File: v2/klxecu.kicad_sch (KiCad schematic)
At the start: 65 parts, among them IC1 SP721, J1 Conn_02x18_Odd_Even, J2 Conn_01x02, J3 Conn_02x04_Counter_Clockwise, J4 Conn_01x01_Male, Q1 2N6517, Q2 STP62NS04Z, Q3 STP62NS04Z, Q4 STP62NS04Z, Q5 STP62NS04Z, Q6 STP62NS04Z, Q7 STP62NS04Z, U1 mega_2560_pro, U2 ERZ-V14D220, U3 LM340T-5.0, U4 ATtiny84-20P, U5 74LS14DR, U6 TC4422AVPA

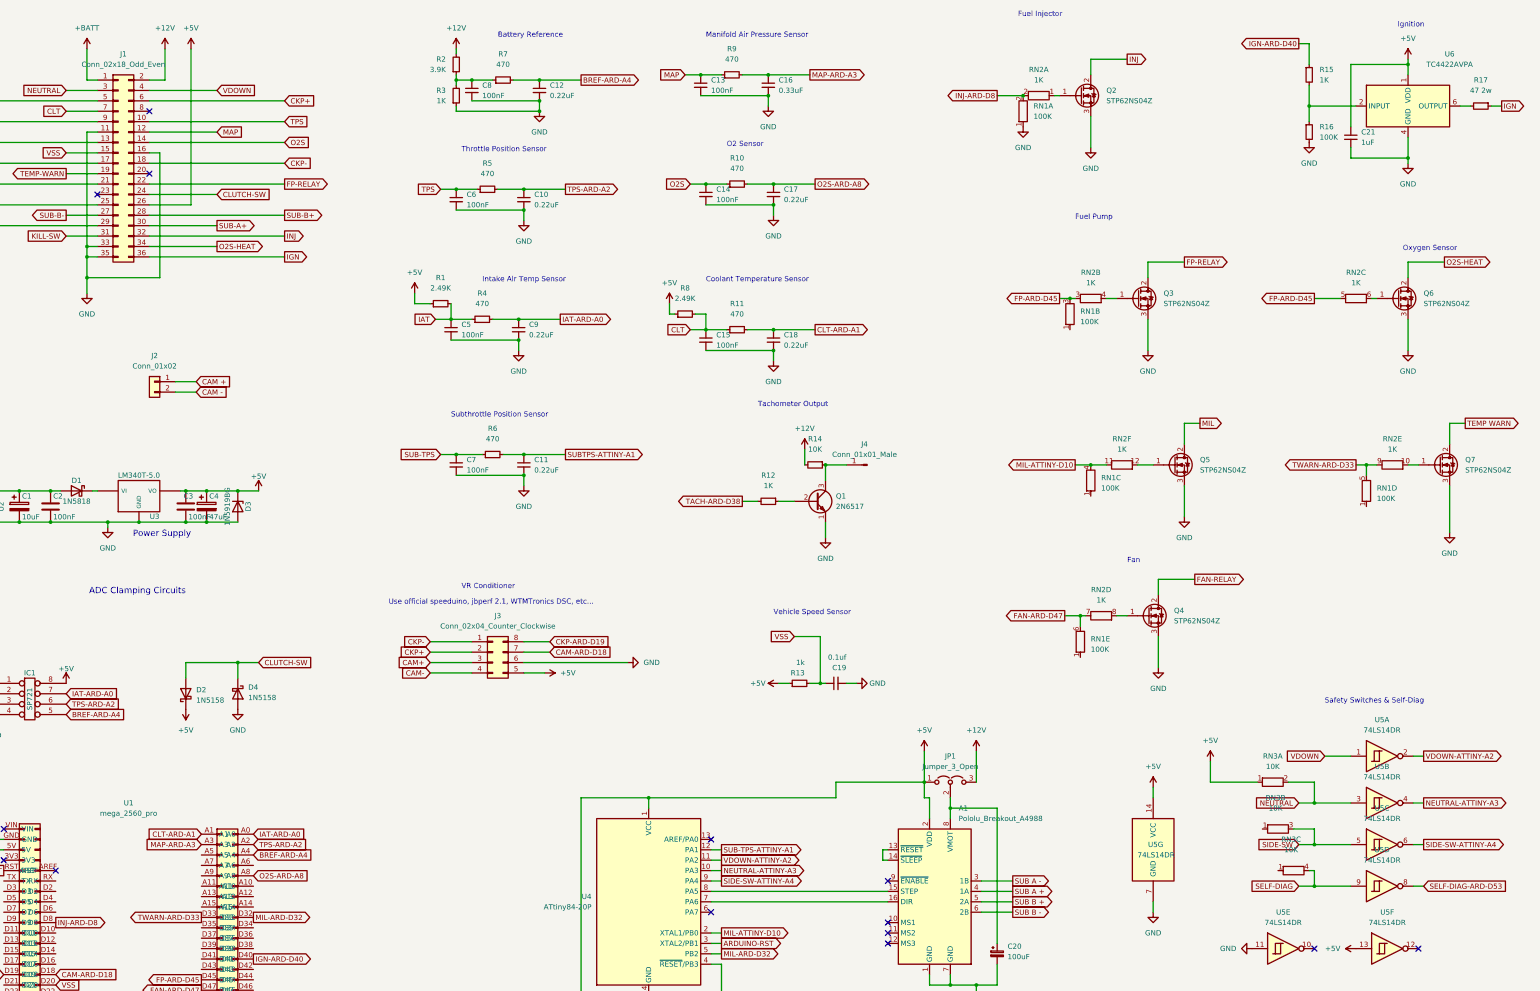
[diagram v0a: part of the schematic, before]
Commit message: Change low current transistors to SMT
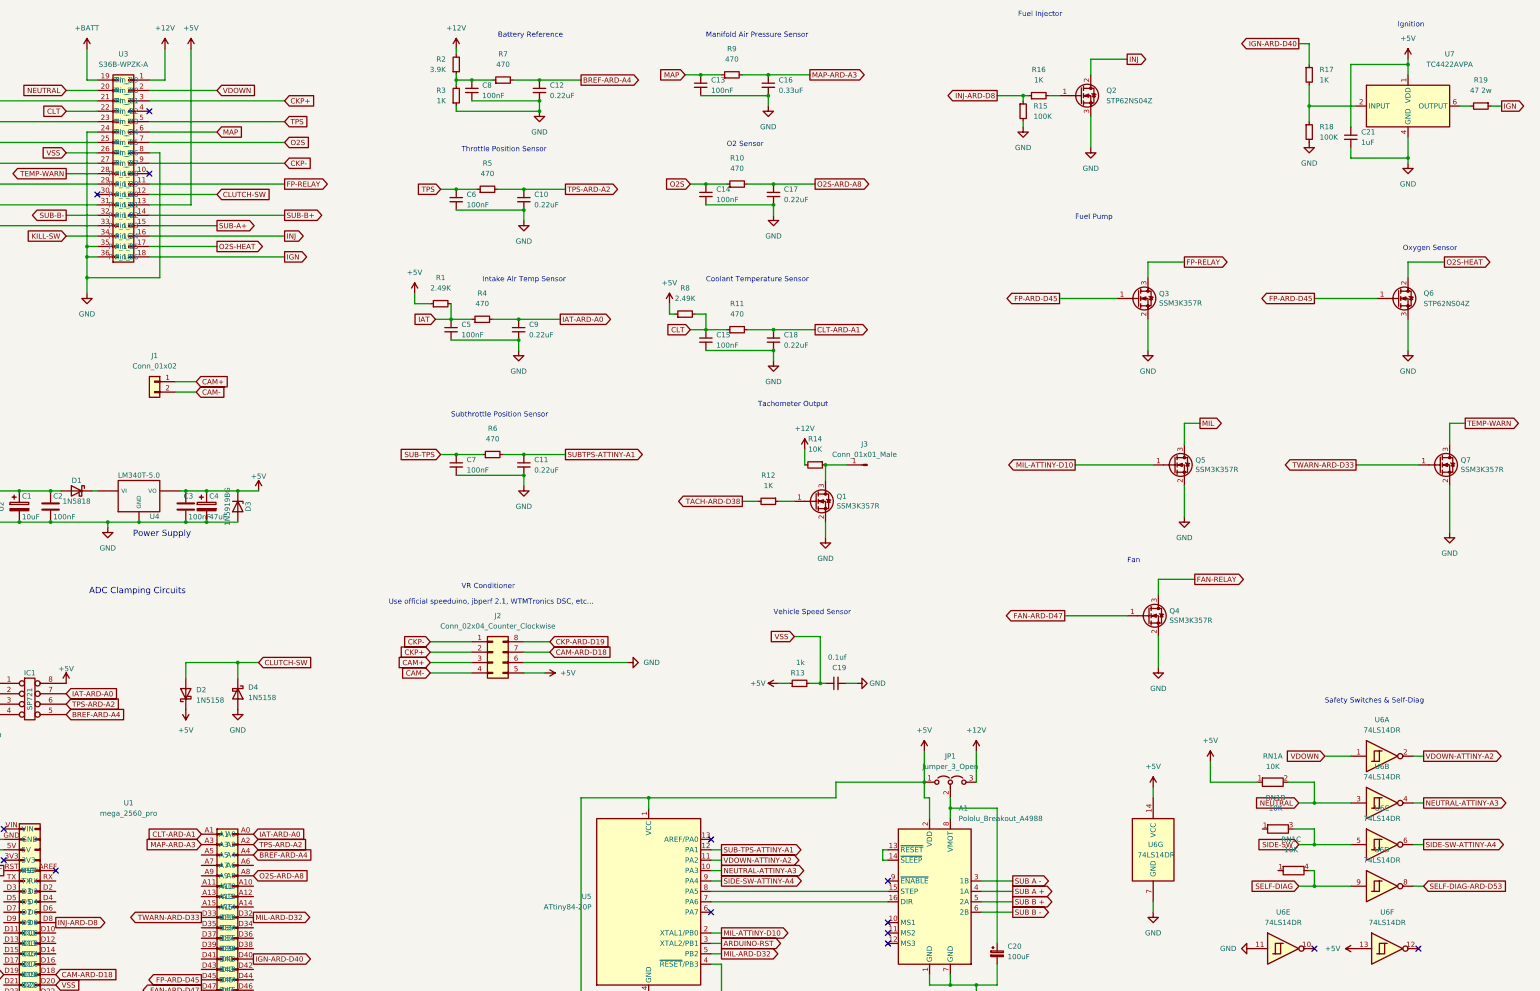
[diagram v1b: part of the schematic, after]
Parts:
- removed J1: Conn_02x18_Odd_Even, Connector_PinHeader_2.54mm:PinHeader_2x18_P2.54mm_Vertical, symbol Connector_Generic:Conn_02x18_Odd_Even
- removed Q1: 2N6517, Package_TO_SOT_THT:TO-92_Inline, symbol Transistor_BJT:2N3904
- removed Q3, Q4, Q5, Q7: STP62NS04Z, Package_TO_SOT_THT:TO-220-3_Vertical, symbol Transistor_FET:BUZ11
- removed RN1: 100K, Resistor_THT:R_Array_SIP6, symbol Device:R_Network05_Split
- removed RN2: 1K, Resistor_THT:R_Array_SIP12, symbol Device:R_Pack06_SIP_Split
- added Q1, Q3, Q4, Q5, Q7: SSM3K357R, Package_TO_SOT_SMD:SOT-23, symbol Transistor_FET:2N7002
- added R15: 100K, Resistor_SMD:R_0805_2012Metric, symbol Device:R_Small
- added R16: 1K, Resistor_SMD:R_0805_2012Metric, symbol Device:R_Small
- added U3: S36B-WPZK-A, mega_2560:S36B-WPZK-A, symbol mega_2560:S36B-WPZK-A
- renumbered J2 to J1, J3 to J2, J4 to J3, R15 to R17, R16 to R18, R17 to R19, RN3 to RN1, U3 to U4, U4 to U5, U5 to U6, U6 to U7
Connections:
- net CAM + is gone; now on net CAM+: J1.1 (Pin_1)
- net CAM - is gone; now on net CAM-: J1.2 (Pin_2)
- net +12V: now also U3.1 (Pin_1)
- net +5V: now also U3.13 (Pin_13)
- net +BATT: now also U3.19 (Pin_19)
- net CKP+: now also U3.3 (Pin_3)
- net CKP-: now also U3.9 (Pin_9)
- net CLT: now also U3.22 (Pin_22)
- net CLUTCH-SW: now also U3.12 (Pin_12)
- net FAN-ARD-D47: now also Q4.1 (G)
- net FAN-RELAY: now also Q4.3 (D), U3.33 (Pin_33)
- net FP-ARD-D45: now also Q6.1 (G), Q3.1 (G)
- net FP-RELAY: now also Q3.3 (D), U3.11 (Pin_11)
- net GND: now also Q1.2 (S), Q3.2 (S), Q4.2 (S), Q5.2 (S), Q7.2 (S), R15.2, U3.24 (Pin_24), U3.35 (Pin_35), U3.36 (Pin_36), U3.8 (Pin_8)
- net IAT: now also U3.25 (Pin_25)
- net IGN: now also U3.18 (Pin_18)
- net INJ: now also U3.16 (Pin_16)
- net INJ-ARD-D8: now also R15.1, R16.1
- net KILL-SW: now also U3.34 (Pin_34)
- net MAP: now also U3.6 (Pin_6)
- net MIL: now also Q5.3 (D), U3.21 (Pin_21)
- net MIL-ATTINY-D10: now also Q5.1 (G)
- net NEUTRAL: now also U3.20 (Pin_20)
- net O2S: now also U3.7 (Pin_7)
- net O2S-HEAT: now also U3.17 (Pin_17)
- net SELF-DIAG: now also U3.23 (Pin_23)
- net SIDE-SW: now also U3.29 (Pin_29)
- net SUB-A+: now also U3.15 (Pin_15)
- net SUB-A-: now also U3.31 (Pin_31)
- net SUB-B+: now also U3.14 (Pin_14)
- net SUB-B-: now also U3.32 (Pin_32)
- net SUB-TPS: now also U3.27 (Pin_27)
- net TEMP-WARN: now also Q7.3 (D), U3.28 (Pin_28)
- net TPS: now also U3.5 (Pin_5)
- net TWARN-ARD-D33: now also Q7.1 (G)
- net VDOWN: now also U3.2 (Pin_2)
- net VSS: now also U3.26 (Pin_26)
- net at J3.1 (Pin_1), R14.1: now also Q1.3 (D)
- net at R12.1: now also Q1.1 (G)
- net at Q2.1 (G): now also R16.2

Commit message: add silkscreen outline for VR conditioner module
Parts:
- J2: footprint Package_DIP:DIP-8_W7.62mm_Socket -> mega_2560:vr_conditioner
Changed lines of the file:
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@@
     (property "Reference" "J2" (id 0) (at 156.21 163.83 0))
     (property "Value" "Conn_02x04_Counter_Clockwise" (id 1) (at 156.21 166.37 0))
-    (property "Footprint" "Package_DIP:DIP-8_W7.62mm_Socket" (id 2) (at 154.94 172.72 0)
+    (property "Footprint" "mega_2560:vr_conditioner" (id 2) (at 154.94 172.72 0)
       (effects (font (size 1.27 1.27)) hide)
     )
@@
     )
     (path "/a4646a71-a41a-457e-b69f-0409bde12e01"
-      (reference "J2") (unit 1) (value "Conn_02x04_Counter_Clockwise") (footprint "Package_DIP:DIP-8_W7.62mm_Socket")
+      (reference "J2") (unit 1) (value "Conn_02x04_Counter_Clockwise") (footprint "mega_2560:vr_conditioner")
     )
     (path "/7efd4165-947a-4227-b367-bffed70d4e31"

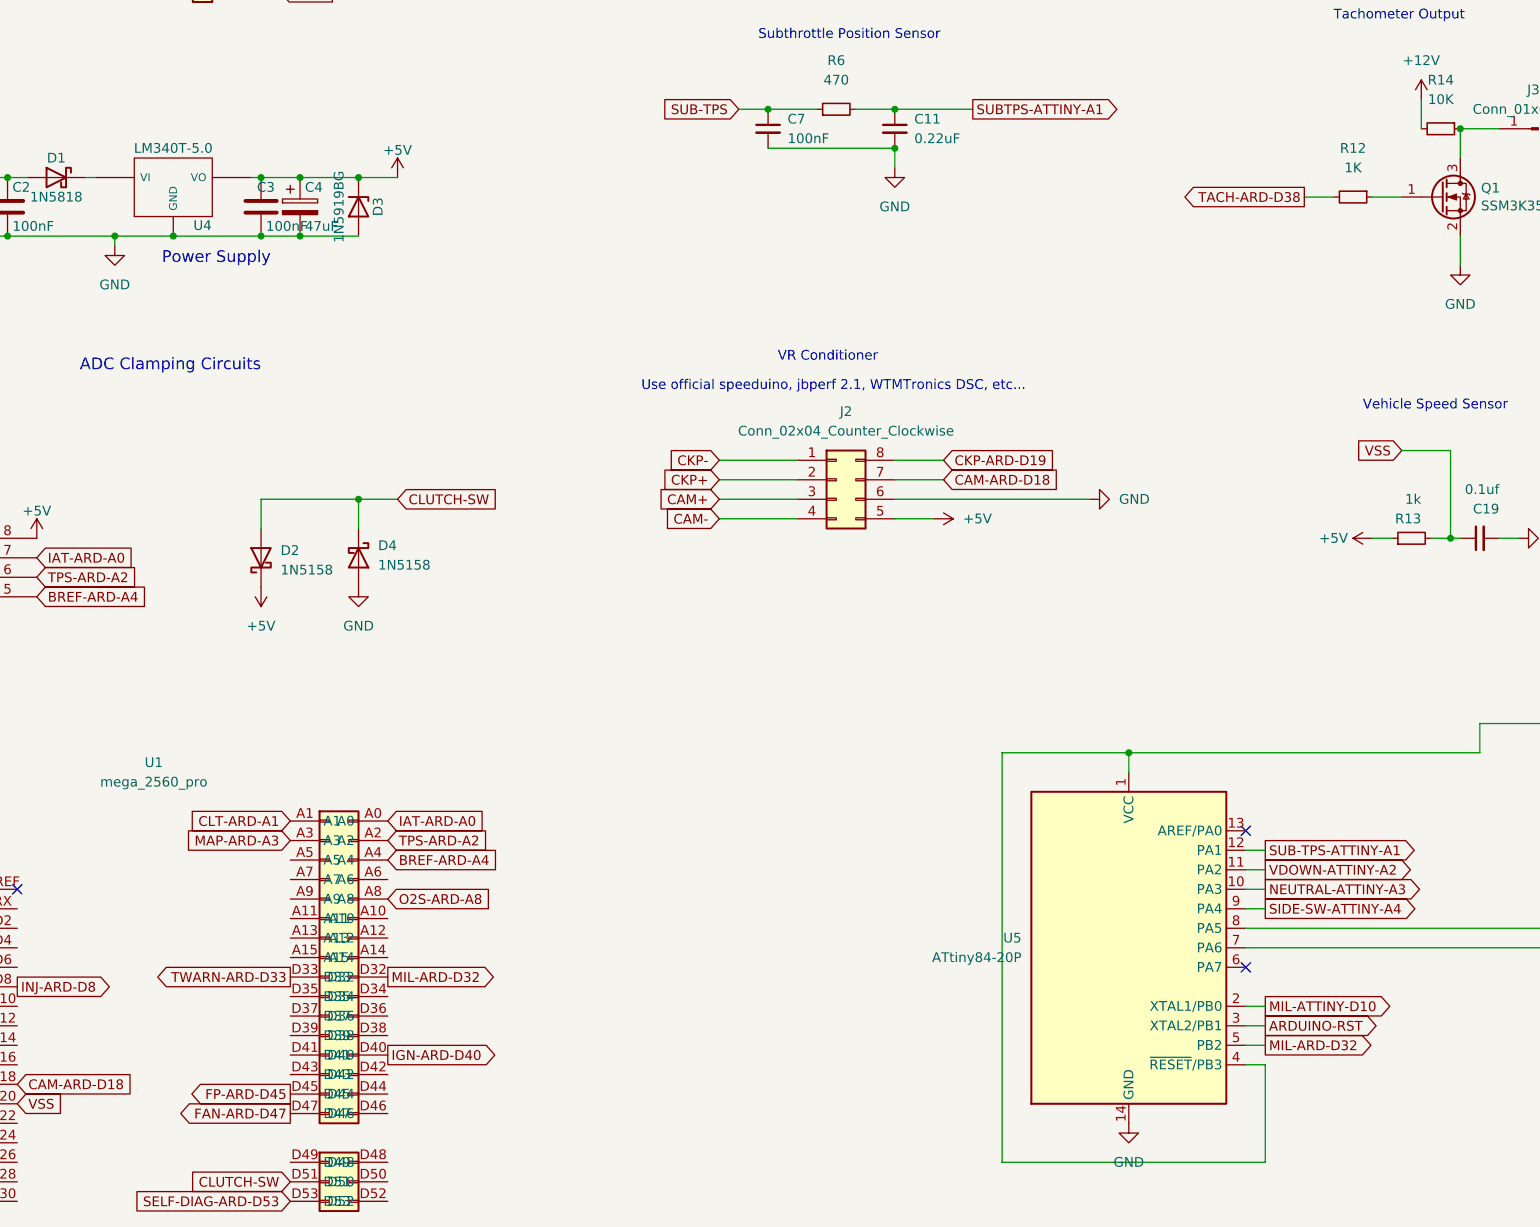
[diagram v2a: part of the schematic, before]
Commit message: fix tach output
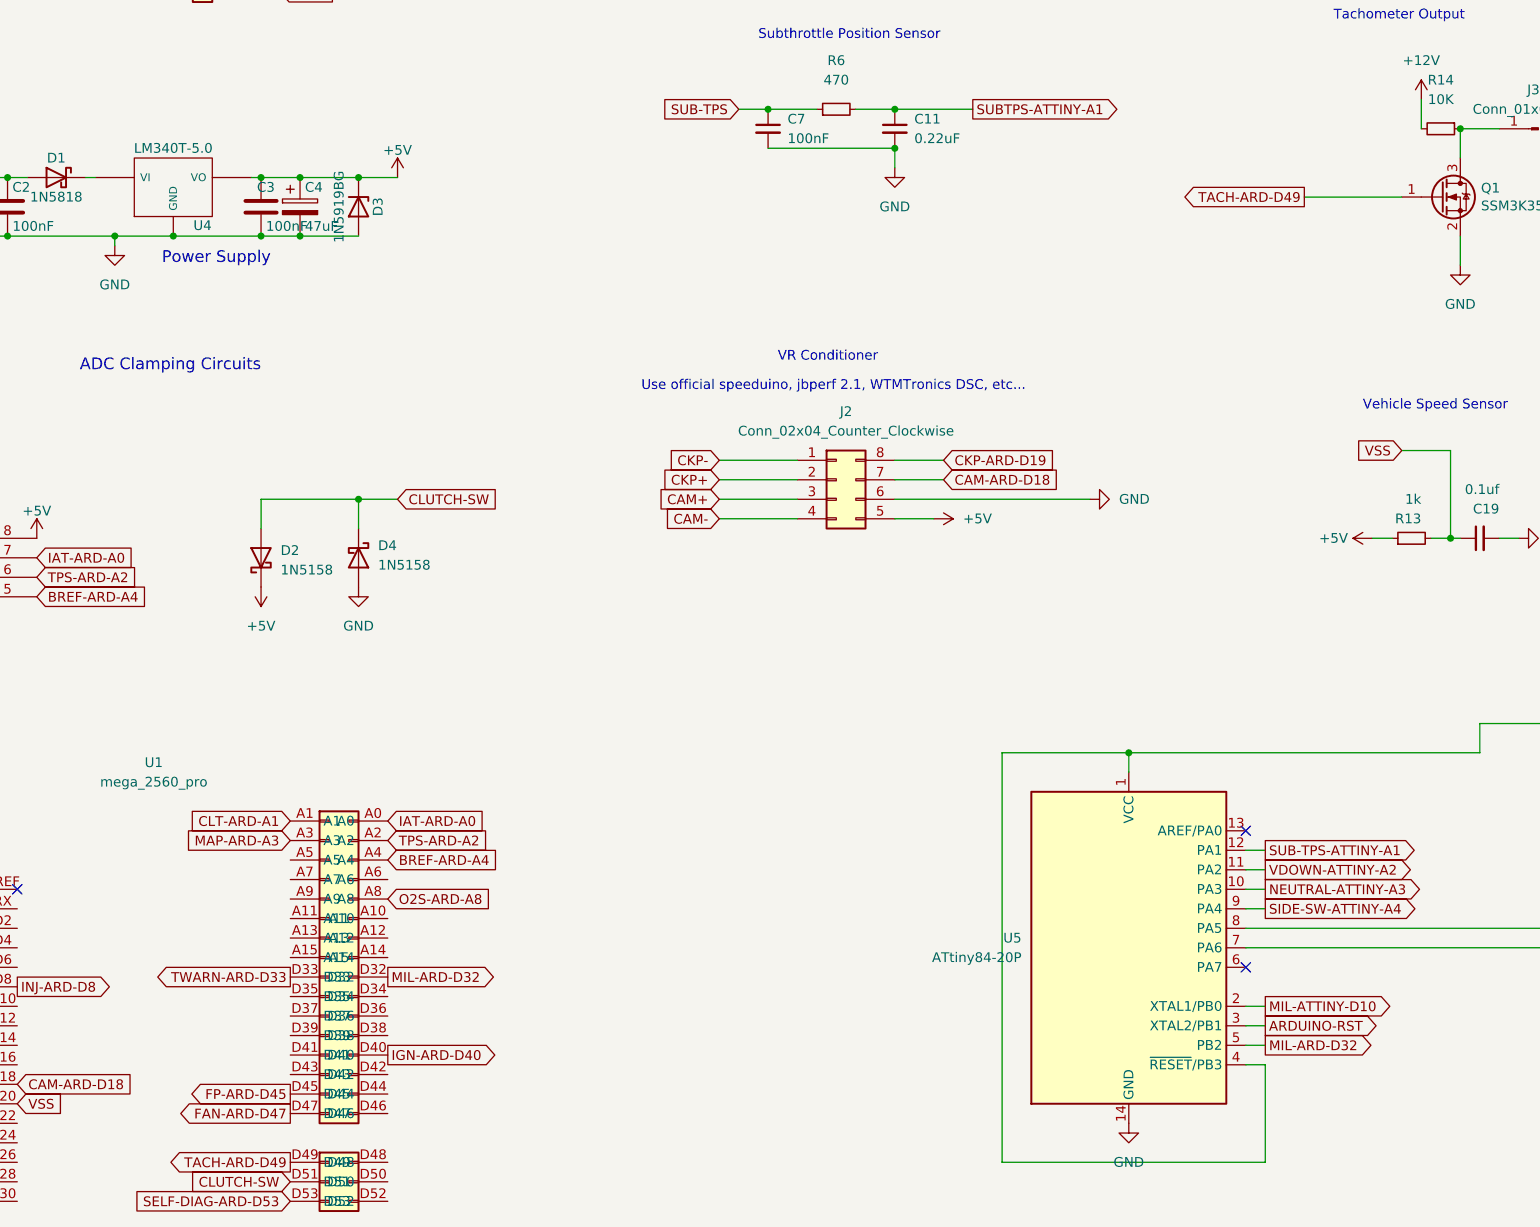
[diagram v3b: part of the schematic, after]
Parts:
- removed R12: 1K, Resistor_SMD:R_0805_2012Metric_Pad1.20x1.40mm_HandSolder, symbol Device:R_Small
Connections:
- net TACH-ARD-D49: now reaches Q1.1 (G)
- net TACH-ARD-D49: now also U1.D49
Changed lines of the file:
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@@
     (stroke (width 0) (type default) (color 0 0 0 0))
   )
-  (wire (pts (xy 215.9 135.89) (xy 219.71 135.89))
-    (stroke (width 0) (type default) (color 0 0 0 0))
-  )
   (wire (pts (xy 55.88 45.72) (xy 55.88 73.66))
     (stroke (width 0) (type default) (color 0 0 0 0))
@@
     (stroke (width 0) (type default) (color 0 0 0 0))
   )
-  (wire (pts (xy 224.79 135.89) (xy 228.6 135.89))
+  (wire (pts (xy 215.9 135.89) (xy 228.6 135.89))
     (stroke (width 0) (type default) (color 0 0 0 0))
   )
@@
     )
   )
-  (global_label "TACH-ARD-D38" (shape output) (at 215.9 135.89 180) (fields_autoplaced)
+  (global_label "TACH-ARD-D49" (shape output) (at 215.9 135.89 180) (fields_autoplaced)
     (effects (font (size 1.27 1.27)) (justify right))
     (property "Intersheet References" "${INTERSHEET_REFS}" (id 0) (at 198.3679 135.8106 0)
@@
     )
   )
+  (global_label "TACH-ARD-D49" (shape output) (at 83.82 261.62 180) (fields_autoplaced)
+    (effects (font (size 1.27 1.27)) (justify right))
+    (property "Intersheet References" "${INTERSHEET_REFS}" (id 0) (at 66.2879 261.5406 0)
+      (effects (font (size 1.27 1.27)) (justify right) hide)
+    )
+  )
   (global_label "NEUTRAL" (shape input) (at 351.79 209.55 180) (fields_autoplaced)
     (effects (font (size 1.27 1.27)) (justify right))
@@
     (pin "1")
   )
-  (symbol (lib_id "Device:R_Small") (at 222.25 135.89 270) (unit 1)
-    (in_bom yes) (on_board yes) (fields_autoplaced)
-    (property "Reference" "R12" (id 0) (at 222.25 129.54 90))
-    (property "Value" "1K" (id 1) (at 222.25 132.08 90))
-    (property "Footprint" "Resistor_SMD:R_0805_2012Metric_Pad1.20x1.40mm_HandSolder" (id 2) (at 222.25 135.89 0)
-      (effects (font (size 1.27 1.27)) hide)
-    )
-    (property "Datasheet" "~" (id 3) (at 222.25 135.89 0)
-      (effects (font (size 1.27 1.27)) hide)
-    )
-    (pin "1")
-    (pin "2")
-  )
   (symbol (lib_id "Transistor_FET:2N7002") (at 386.08 127 0) (unit 1)
     (in_bom yes) (on_board yes)
@@
       (reference "R11") (unit 1) (value "470") (footprint "Resistor_SMD:R_0805_2012Metric_Pad1.20x1.40mm_HandSolder")
     )
-    (path "/3760ca5e-45d5-4ae9-964e-bc7541bdaff8"
-      (reference "R12") (unit 1) (value "1K") (footprint "Resistor_SMD:R_0805_2012Metric_Pad1.20x1.40mm_HandSolder")
-    )
     (path "/7b0073f7-f5a3-48c9-a30a-a4bf367c7a44"

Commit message: create custom symbol for schmitt trigger & fix label for subthrottle stepper output
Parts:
- removed RN1: 10K, Resistor_THT:R_Array_SIP4, symbol Device:R_Network03_Split
- removed U6: 74LS14DR, Package_SO:SOIC-14_3.9x8.7mm_P1.27mm, symbol 74xx:74LS14
- added C?: 0.1uF, symbol Device:C_Small
- added RN?: 10k, Resistor_THT:R_Array_SIP4, symbol Device:R_Network03
- added U?: 74xx14, symbol mega_2560:74xx14
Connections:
- net SUB A + is gone; now on net SUB-A+: A1.4 (1A)
- net SUB A - is gone; now on net SUB-A-: A1.3 (1B)
- net SUB B - is gone; now on net SUB-B-: A1.6 (2B)
- net SUBTPS-ATTINY-A1 is gone; now on net SUB-TPS-ATTINY-A1: C11.1, R6.2
- net +5V: now also C?.1, RN?.1 (common), U?.14 (Vcc)
- net GND: now also C?.2, U?.11, U?.13, U?.7 (GND)
- net NEUTRAL: now also RN?.4 (R3), U?.3
- net NEUTRAL-ATTINY-A3: now also U?.4
- net SELF-DIAG: now also RN?.2 (R1), U?.9
- net SELF-DIAG-ARD-D53: now also U?.8
- net SIDE-SW: now also RN?.3 (R2), U?.5
- net SIDE-SW-ATTINY-A4: now also U?.6
- net VDOWN: now also U?.1
- net VDOWN-ATTINY-A2: now also U?.2
- net SUB B + renamed SUB-B +
